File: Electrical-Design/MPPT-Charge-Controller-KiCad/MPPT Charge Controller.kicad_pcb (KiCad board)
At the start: 4 copper layers, 38.7 x 60 mm, 53 parts, among them Q1 SI7272DP, Q3 2N7002, U2 AP63203WU, U3 ACS712-20A, U4 ACS712-20A, U5 MCP4018

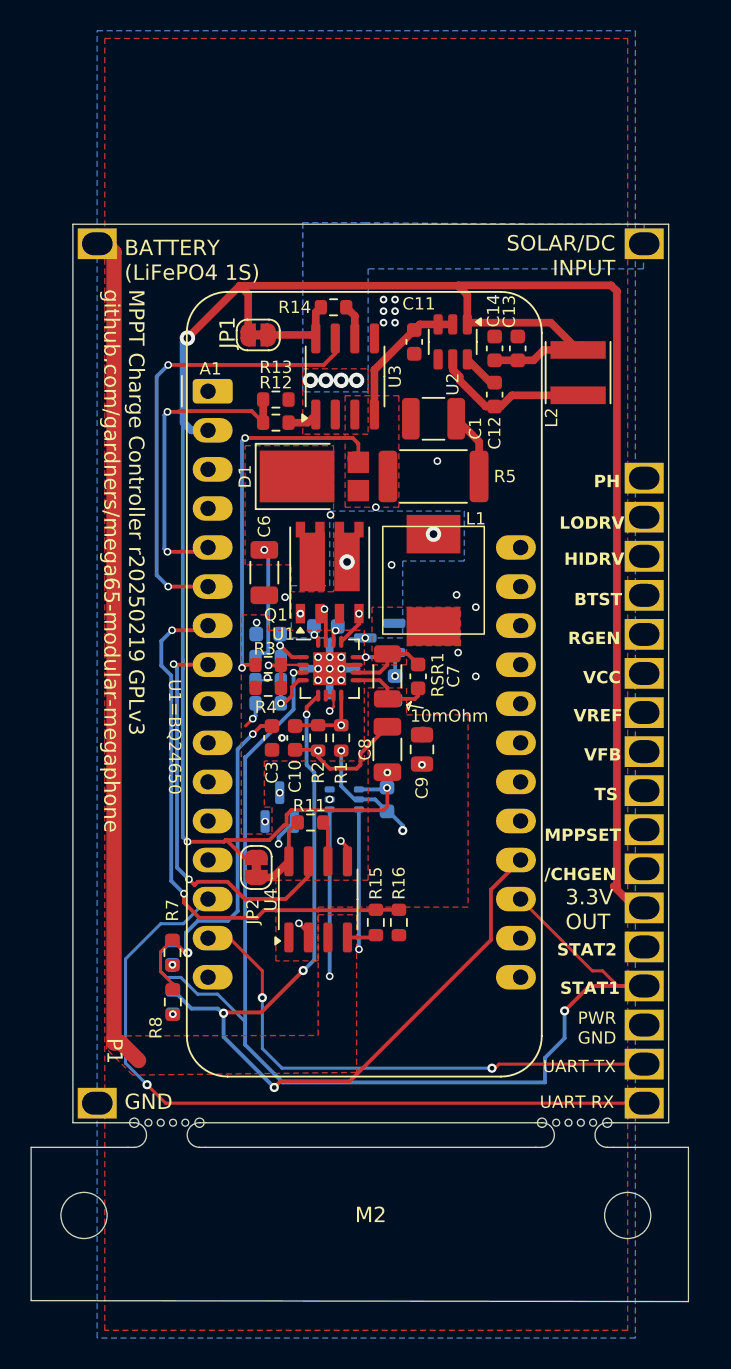
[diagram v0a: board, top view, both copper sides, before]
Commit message: Update schematics - delete tracks - 4 layer boards have only 2 signal layers
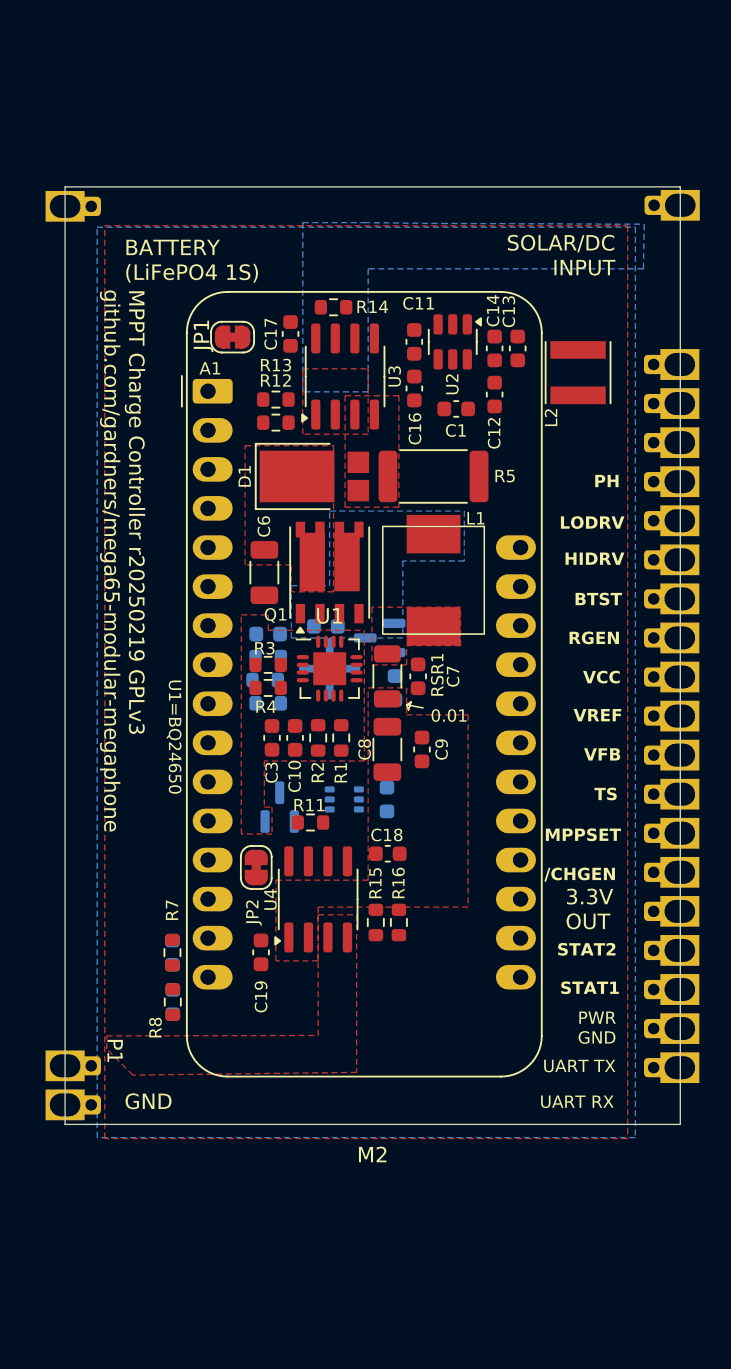
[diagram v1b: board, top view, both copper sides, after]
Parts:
- added C16: 2.2uF, Capacitor_SMD:C_0603_1608Metric, F.Cu at (113.1, 79.2)
- added C17: 0.1uF, Capacitor_SMD:C_0603_1608Metric, F.Cu at (105.1, 75.7)
- added C18: 2.2uF, Capacitor_SMD:C_0603_1608Metric, F.Cu at (111.4, 109.5)
- added C19: 0.1uF, Capacitor_SMD:C_0603_1608Metric, F.Cu at (103.2, 115.9)
- C1: footprint Capacitor_SMD:C_1210_3225Metric -> Capacitor_SMD:C_0603_1608Metric
- C2: value C2=1uF -> 1uF
- C9: footprint Capacitor_SMD:C_0805_2012Metric -> Capacitor_SMD:C_0603_1608Metric
- M2: footprint MegaCastle:MegaCastle2x23-Module-I30.0x53.6-M80000307FFFC-PANEL-NIBBLE -> MPPT Charge Controller Footprint Library:MegaCastle2x24-Module-I40.0x56.2-M8000030FFFFF-SPAREPAD
- R10: value R10=30.1k -> 30.1k
- R5: value 2 Ohm -> 2
- R6: value R6=10 -> 10
- R9: value R9=5.23k -> 5.23k
- RSR1: value 10mOhm -> 0.01
- U3, U4: value ACS712-20A -> ACS712
- moved JP1 1.67 mm to (101.3, 75.9)
- moved C1 1.61 mm to (115.8, 80.6)
- moved M2 1.17 mm to (110.4, 96.6)
- moved R9 0.20 mm to (103.4, 98.2)
- turned R14 to 0 degrees
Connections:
- C11 pad 2: /VIN -> /VCC
- C15 pad 2: PWR_GND -> GND
- C2 pad 2: PWR_GND -> GND
- C3 pad 2: PWR_GND -> GND
- D1 pad 2: /VIN -> /VCC
- M2 pad 23: GND -> unconnected-(M2-Pad23)
- M2 pad 24: /Input -> GND
- M2 pad 30: /PH -> unconnected-(M2-Pad30)
- M2 pad 31: /LODRV -> /SD_CS
- M2 pad 32: /HIDRV -> /PH
- M2 pad 33: /BTST -> /LODRV
- M2 pad 34: /RGEN -> /HIDRV
- M2 pad 35: /VCC -> /BTST
- M2 pad 36: /VREF -> /RGEN
- M2 pad 37: /VFB -> /VCC
- M2 pad 38: /TS -> /VREF
- M2 pad 39: /MPPSET -> /VFB
- M2 pad 40: /~{Charge EN} -> /TS
- M2 pad 41: +3.3V -> /MPPSET
- M2 pad 42: /STAT2 -> /~{Charge EN}
- M2 pad 43: /STAT1 -> +3.3V
- M2 pad 44: PWR_GND -> /STAT2
- M2 pad 45: UART_TX -> /STAT1
- M2 pad 46: UART_RX -> GND
- NT1 pad 1: PWR_GND -> GND
- NT2 pad 1: PWR_GND -> GND
- NT3 pad 1: PWR_GND -> GND
- NT4 pad 1: PWR_GND -> GND
- Q3 pad 2: PWR_GND -> GND
- R1 pad 2: PWR_GND -> GND
- R10 pad 2: PWR_GND -> GND
- R14 pad 1: Net-(U3-FILTER) -> VCC_ACS712
- R14 pad 2: VCC_ACS712 -> Net-(U3-~FAULT)
- R3 pad 1: /VIN -> /VCC
- R4 pad 1: /MPPSET -> /VREF
- R4 pad 2: PWR_GND -> GND
- R5 pad 1: /VIN -> /VCC
- R7 pad 1: /VREF -> /VCC
- R8 pad 1: /VREF -> /VCC
- U1 pad 11: PWR_GND -> GND
- U1 pad 17: PWR_GND -> GND
- U2 pad 2: /VIN -> /VCC
- U2 pad 3: /VIN -> /VCC
- U3 pad 3: /VIN -> /VCC
- U3 pad 4: /VIN -> /VCC
- U3 pad 6: Net-(U3-FILTER) -> Net-(U3-~FAULT)
- U5 pad 2: PWR_GND -> GND
- U5 pad 5: /MPPSET -> /VREF
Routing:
- net +3.3V: track 146.3 -> 0.00 mm, vias 3 -> 0
- net /STAT1: track 79.1 -> 0.00 mm, vias 2 -> 0
- net /STAT2: track 69.8 -> 0.00 mm, vias 4 -> 0
- net VBAT_OUT: track 56.7 -> 0.00 mm
- net UART_RX: track 48.6 -> 0.00 mm, vias 1 -> 0
- net /VREF: track 48.5 -> 0.00 mm, vias 4 -> 0
- net /MPPSET: track 37.4 -> 0.00 mm, vias 3 -> 0
- net /Battery Voltage: track 35.7 -> 0.00 mm, vias 2 -> 0
- net UART_TX: track 34.9 -> 0.00 mm, vias 2 -> 0
- net /VCC: track 34.8 -> 0.00 mm, vias 4 -> 0
- net /VIN: track 34.3 -> 0.00 mm, vias 2 -> 0
- net PWR_GND: track 32.7 -> 0.00 mm, vias 14 -> 0
- net /TS: track 31.1 -> 0.00 mm, vias 2 -> 0
- net /HIDRV: track 30.0 -> 0.00 mm, vias 2 -> 0
- net /Solar Current: track 29.8 -> 0.00 mm, vias 2 -> 0
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- added copper zone on F.Cu, net /VCC
- removed copper zone on F.Cu, net /VIN
- removed copper zone on B.Cu, net PWR_GND
- removed copper zone on F.Cu, net PWR_GND
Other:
- board size 38.7 x 60 mm -> 40 x 61 mm

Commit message: Routing, adding schematics
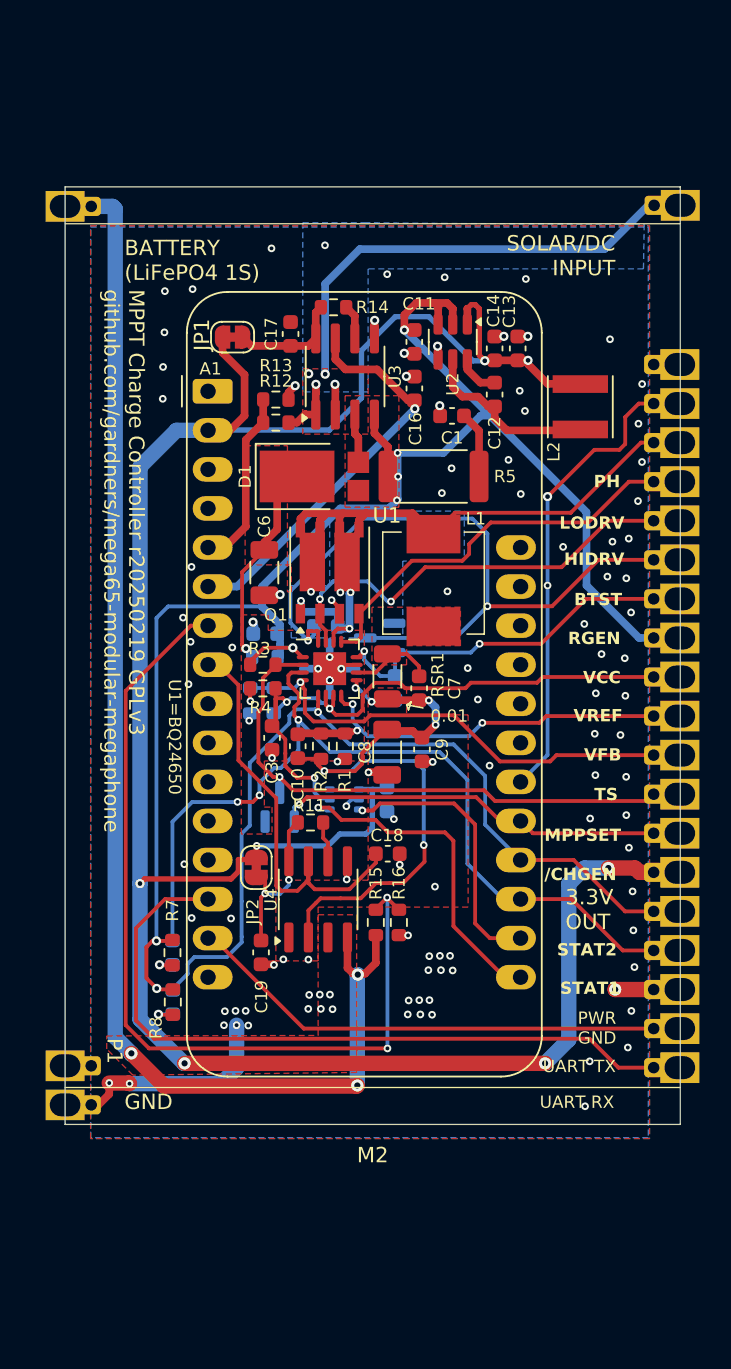
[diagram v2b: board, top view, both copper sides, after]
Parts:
- moved L2 2.22 mm to (123.9, 80.4)
- moved R9 1.45 mm to (104.0, 99.5), turned to 90 degrees
- moved R10 1.18 mm to (102.5, 99.5), turned to -90 degrees
- moved C7 0.77 mm to (113.4, 98.7)
- moved R1 0.59 mm to (108.6, 102.5)
- moved R2 0.57 mm to (107.1, 102.5)
- moved C10 0.57 mm to (105.5, 102.5)
- moved C1 0.52 mm to (115.6, 81.0)
- moved R4 0.35 mm to (103.3, 98.7)
- moved R3 0.35 mm to (103.3, 97.2)
- moved R6 0.22 mm to (103.4, 96.7)
- moved C2 0.20 mm to (103.4, 95.2)
- moved C8 0.18 mm to (111.4, 102.9)
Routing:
- net +3.3V: track 0.00 -> 154.2 mm, vias 0 -> 7
- net /VCC: track 0.00 -> 110.3 mm, vias 0 -> 7
- net VBAT_OUT: track 0.00 -> 85.9 mm, vias 0 -> 3
- net /Battery Voltage: track 0.00 -> 58.5 mm, vias 0 -> 2
- net /STAT1: track 0.00 -> 57.4 mm, vias 0 -> 3
- net /STAT2: track 0.00 -> 55.6 mm, vias 0 -> 1
- net /BTST: track 0.00 -> 47.5 mm, vias 0 -> 2
- net UART_RX: track 0.00 -> 46.4 mm
- net Net-(U1-SRN): track 0.00 -> 43.4 mm, vias 0 -> 6
- net GND: track 0.00 -> 43.1 mm, vias 0 -> 115
- net /PH: track 0.00 -> 42.3 mm, vias 0 -> 5
- net /VREF: track 0.00 -> 41.6 mm, vias 0 -> 3
- net /MPPSET: track 0.00 -> 36.5 mm, vias 0 -> 1
- net /Input: track 0.00 -> 35.3 mm, vias 0 -> 4
- net UART_TX: track 0.00 -> 31.4 mm
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- added copper zone on In1.Cu, net GND
- added copper zone on In2.Cu, net GND

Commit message: Routing
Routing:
- net GND: track 43.1 -> 69.4 mm, vias 115 -> 116
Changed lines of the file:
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@@
 		)
 		(property "Value" "22uF"
-			(at 0.025 -0.025 -90)
+			(at 0.025 -0.025 270)
 			(layer "B.SilkS")
 			(effects
@@
 	)
 	(segment
+		(start 124.16 116.28)
+		(end 126.19 118.31)
+		(width 0.25)
+		(layer "F.Cu")
+		(net 22)
+	)
+	(segment
 		(start 114.805 81.01)
 		(end 114.805 80.375)
@@
 	)
 	(segment
+		(start 109.41 107.47)
+		(end 111.36 107.47)
+		(width 0.25)
+		(layer "F.Cu")
+		(net 22)
+	)
+	(segment
 		(start 109.375 97.2)
 		(end 108.625 97.2)
@@
 	)
 	(segment
+		(start 118.6 116.28)
+		(end 124.16 116.28)
+		(width 0.25)
+		(layer "F.Cu")
+		(net 22)
+	)
+	(segment
 		(start 102.455 99.285)
 		(end 102.455 99.545)
@@
 	)
 	(segment
+		(start 108.71 106.77)
+		(end 109.41 107.47)
+		(width 0.25)
+		(layer "F.Cu")
+		(net 22)
+	)
+	(segment
+		(start 108.71 106.39)
+		(end 108.71 106.77)
+		(width 0.25)
+		(layer "F.Cu")
+		(net 22)
+	)
+	(segment
 		(start 118.36 75.84)
 		(end 118.35 75.85)
@@
 	)
 	(segment
+		(start 111.36 107.47)
+		(end 111.95 106.88)
+		(width 0.25)
+		(layer "F.Cu")
+		(net 22)
+	)
+	(segment
 		(start 102.455 99.545)
 		(end 102.47 99.56)
@@
 	)
 	(segment
+		(start 111.95 106.88)
+		(end 114.69 106.88)
+		(width 0.25)
+		(layer "F.Cu")
+		(net 22)
+	)
+	(segment
 		(start 107.625 97.45)
 		(end 106.875 97.45)
@@
 	)
 	(segment
+		(start 116.42 114.1)
+		(end 118.6 116.28)
+		(width 0.25)
+		(layer "F.Cu")
+		(net 22)
+	)
+	(segment
+		(start 116.42 108.61)
+		(end 116.42 114.1)
+		(width 0.25)
+		(layer "F.Cu")
+		(net 22)
+	)
+	(segment
 		(start 114.805 80.375)
 		(end 114.78 80.35)
@@
 	)
 	(segment
+		(start 114.69 106.88)
+		(end 114.95 107.14)
+		(width 0.25)
+		(layer "F.Cu")
+		(net 22)
+	)
+	(segment
+		(start 114.95 107.14)
+		(end 116.42 108.61)
+		(width 0.25)
+		(layer "F.Cu")
+		(net 22)
+	)
+	(segment
 		(start 114.675 77.3375)
 		(end 114.675 76.515)
@@
 	)
 	(via
-		(at 111.8 107.23)
+		(at 111.95 106.88)
 		(size 0.5)
 		(drill 0.25)
@@
 	)
 	(via
+		(at 114.95 107.14)
+		(size 0.5)
+		(drill 0.25)
+		(layers "F.Cu" "B.Cu")
+		(net 22)
+	)
+	(via
 		(at 98.65 113.66)
 		(size 0.5)
@@
 	)
 	(segment
-		(start 111.8 107.23)
-		(end 111.8 107.175)
-		(width 0.25)
-		(layer "B.Cu")
-		(net 22)
-	)
-	(segment
 		(start 101.57 123.42)
 		(end 101.57 120.63)
@@
 	)
 	(segment
+		(start 111.95 106.88)
+		(end 111.505 106.88)
+		(width 0.25)
+		(layer "B.Cu")
+		(net 22)
+	)
+	(segment
 		(start 102.39 100.83)
 		(end 102.39 100.63)
@@
 	)
 	(segment
+		(start 111.505 106.88)
+		(end 111.35 106.725)
+		(width 0.25)
+		(layer "B.Cu")
+		(net 22)
+	)
+	(segment
 		(start 102.85 94.975)
 		(end 102.85 94.63)
@@
 	)
 	(segment
-		(start 111.8 107.175)
-		(end 111.35 106.725)
-		(width 0.25)
-		(layer "B.Cu")
-		(net 22)
-	)
-	(segment
 		(start 109.04 105.95)
 		(end 109.525 105.95)
@@
 	)
 	(segment
-		(start 120.035 117.51)
-		(end 118.99 117.51)
-		(width 0.25)
-		(layer "F.Cu")
-		(net 48)
-	)
-	(segment
-		(start 115.67 114.19)
-		(end 115.67 108.64)
+		(start 118.99 117.51)
+		(end 115.67 114.19)
 		(width 0.25)
 		(layer "F.Cu")
@@
 	)
 	(segment
-		(start 111.41 108.09)
-		(end 110.6 107.28)
+		(start 120.035 117.51)
+		(end 118.99 117.51)
 		(width 0.25)
 		(layer "F.Cu")
@@
 	)
 	(segment
-		(start 118.99 117.51)
-		(end 115.67 114.19)
+		(start 115.67 108.64)
+		(end 115.12 108.09)
 		(width 0.25)
 		(layer "F.Cu")
@@
 	)
 	(segment
-		(start 110.6 107.28)
-		(end 108.39 107.28)
+		(start 115.67 114.19)
+		(end 115.67 108.64)
 		(width 0.25)
 		(layer "F.Cu")
@@
 	)
 	(segment
-		(start 115.12 108.09)
-		(end 111.41 108.09)
+		(start 109.2 108.09)
+		(end 107.59 106.48)
 		(width 0.25)
 		(layer "F.Cu")
@@
 	)
 	(segment
-		(start 108.39 107.28)
-		(end 107.59 106.48)
-		(width 0.25)
-		(layer "F.Cu")
-		(net 48)
-	)
-	(segment
-		(start 115.67 108.64)
-		(end 115.12 108.09)
+		(start 115.12 108.09)
+		(end 109.2 108.09)
 		(width 0.25)
 		(layer "F.Cu")
